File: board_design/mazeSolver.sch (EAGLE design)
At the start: 12 parts, among them IC1 L293DD, IC2 CP2101, J1 1-2295018-2, U1 ESP-WROOM-32, U2 AP1509-SOP8L

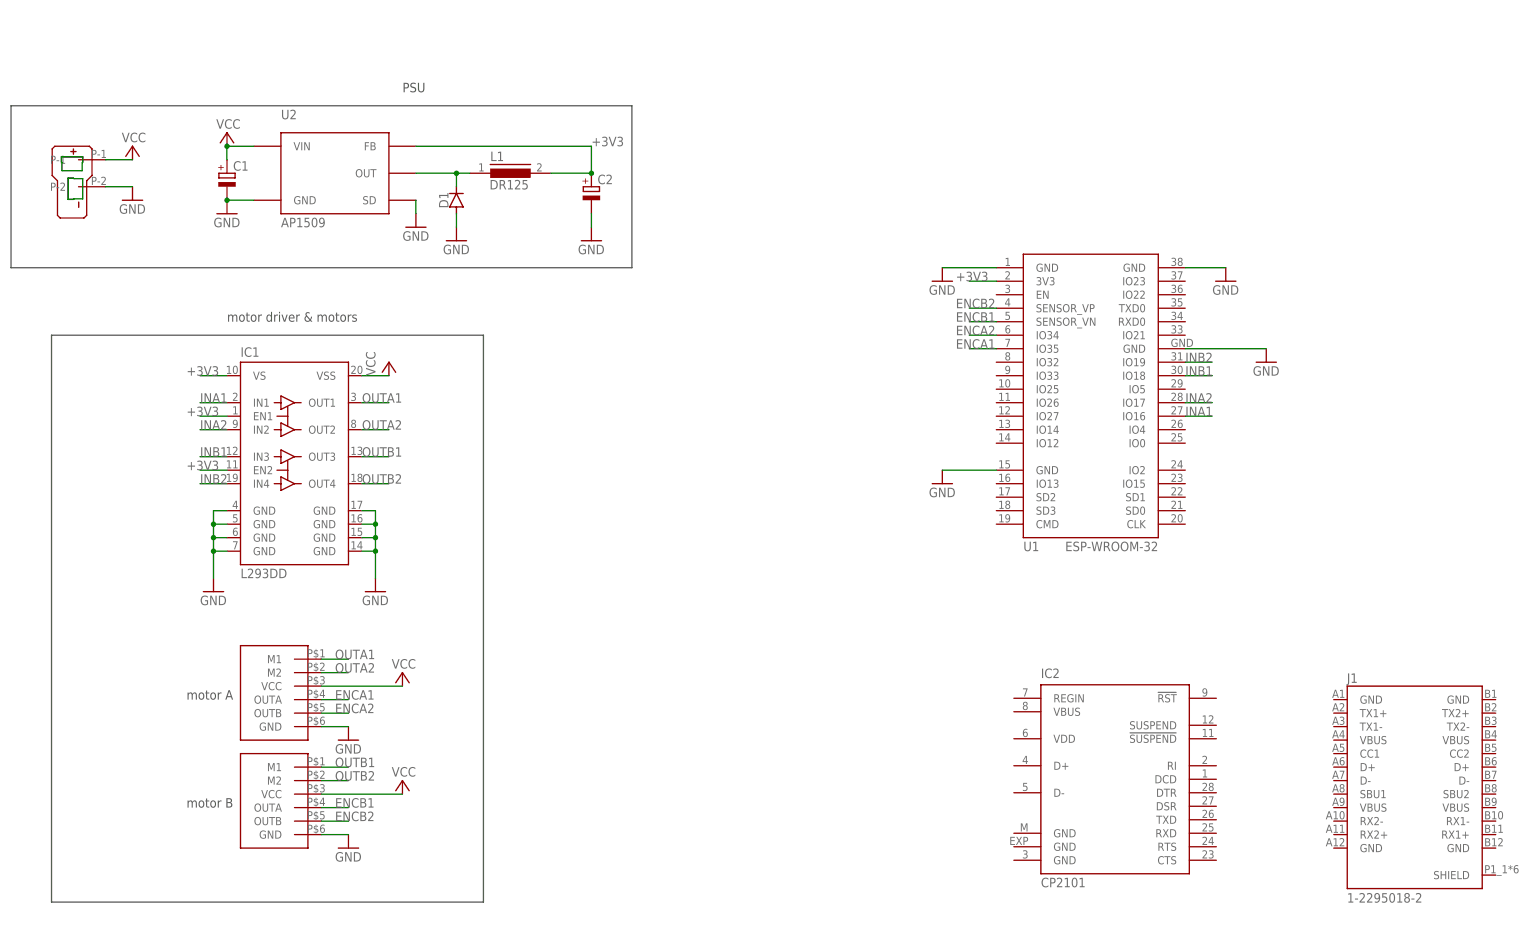
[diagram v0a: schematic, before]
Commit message: USB and reset circuitry.
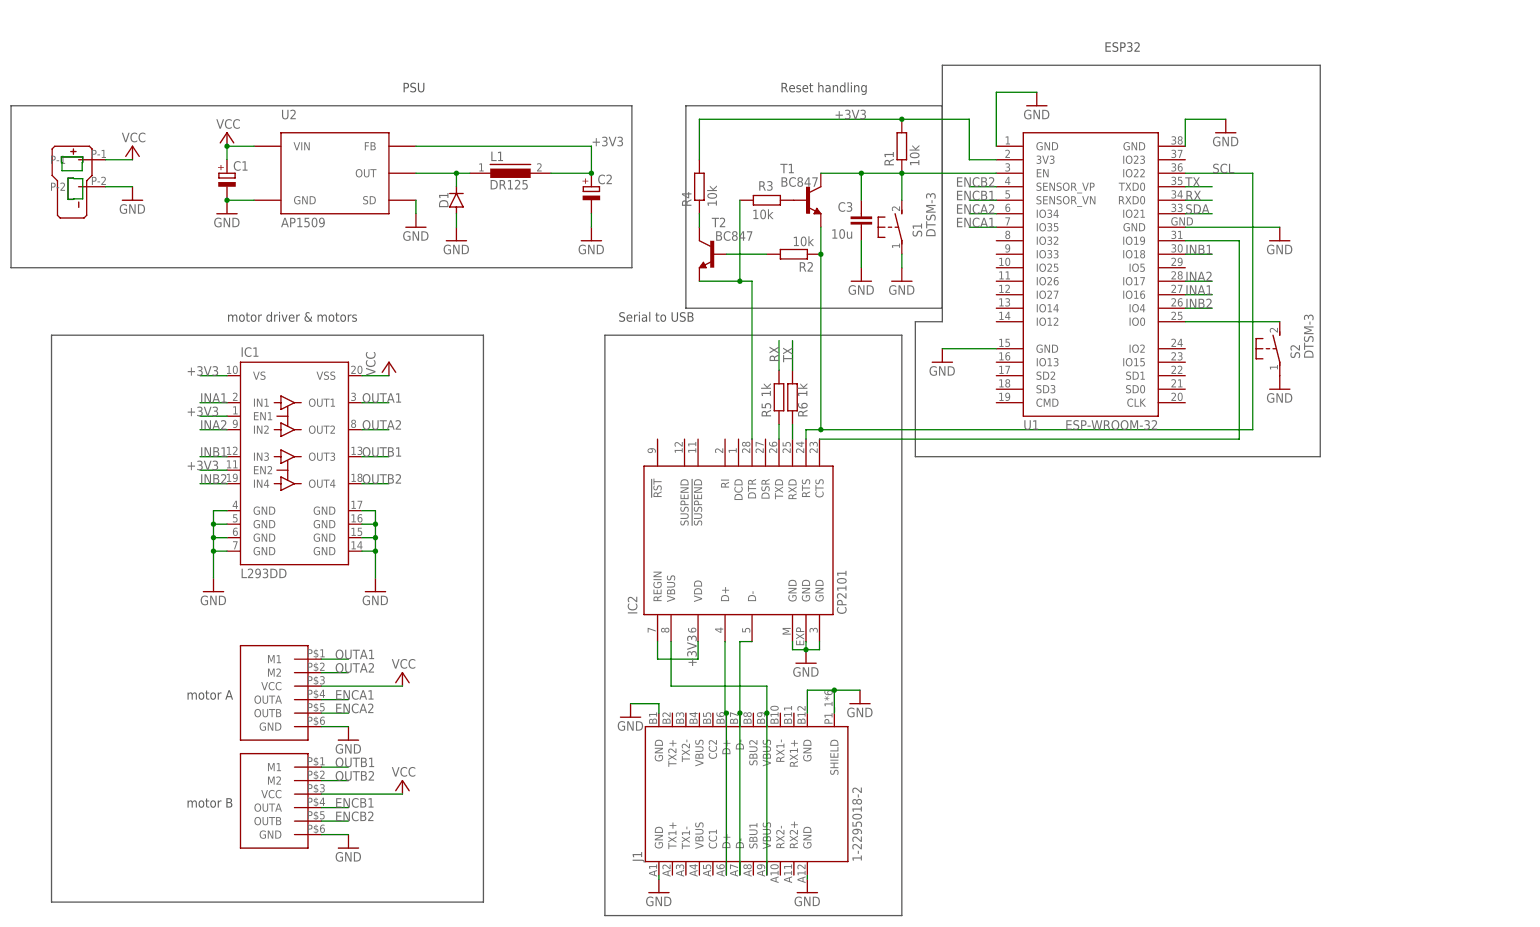
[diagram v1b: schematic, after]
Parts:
- added C3: 10u, rcl:C-EUC1206
- added R1, R2, R3, R4: 10k, rcl:R-EU_R1206
- added R5, R6: 1k, rcl:R-EU_R1206
- added S1, S2: DTSM-3, switch-tact:DTSM-3
- added T1, T2: BC847, transistor:BC847
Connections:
- new net N$1: C3.1, R1.1, S1.2, T1.C, U1.EN
- new net N$10: IC2.D+, J1.D+, J1.D+@1
- new net N$11: IC2.VBUS, J1.VBUS@2, J1.VBUS@4
- new net N$12: IC2.CTS, U1.IO19
- new net N$13: S2.2, U1.IO0
- new net N$2: R3.1, T1.B
- new net N$4: IC2.D-, J1.D-, J1.D-@1
- new net N$5: R2.2, T2.B
- new net N$6: R4.1, T2.C
- new net N$7: IC2.DTR, R3.2, T2.E
- new net N$8: IC2.TXD, R5.1
- new net N$9: IC2.RXD, R6.1
- new net RX: R5.2, U1.RXD0
- new net SCL: IC2.RTS, R2.1, T1.E, U1.IO22
- new net SDA: U1.IO21
- new net TX: R6.2, U1.TXD0
- net +3V3: now also IC2.REGIN, IC2.VDD, R1.2, R4.2
- net GND: now also C3.2, IC2.GND, IC2.GND@EXP, IC2.GND@M, J1.GND@1, J1.GND@2, J1.GND@3, J1.GND@4, J1.SHIELD, S1.1, S2.1
- net INB2: now also U1.IO4; no longer U1.IO19
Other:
- note added: "ESP32"
- note added: "Reset handling"
- note added: "Serial to USB"
- moved on the sheet: IC2, J1, U1

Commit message: Finished schematic
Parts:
- removed C3: 10u, rcl:C-EUC1206
- removed IC2: CP2101, silabs-2:CP2101
- removed J1: 1-2295018-2, 1-2295018-2:1-2295018-2
- removed R1, R2, R3, R4: 10k, rcl:R-EU_R1206
- removed R5, R6: 1k, rcl:R-EU_R1206
- removed S1, S2: DTSM-3, switch-tact:DTSM-3
- removed T1, T2: BC847, transistor:BC847
- removed U1: ESP-WROOM-32, esp32:ESP-WROOM-32
- added C4: 10u, rcl:C-EUC1206
- added IC3: CP2101, silabs-2:CP2101
- added J2: 1-2295018-2, 1-2295018-2:1-2295018-2
- added R10, R7, R8, R9: 10k, rcl:R-EU_R1206
- added R11, R12: 1k, rcl:R-EU_R1206
- added S3, S4: DTSM-3, switch-tact:DTSM-3
- added T3, T4: BC847, transistor:BC847
- added U$4: TDA9548, tda9548:TDA9548
- added U$5, U$6, U$7: VL6180X, vl6180x:VL6180X
- added U3: ESP-WROOM-32, esp32:ESP-WROOM-32
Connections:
- removed net N$10: IC2.D+, J1.D+, J1.D+@1
- removed net N$11: IC2.VBUS, J1.VBUS@2, J1.VBUS@4
- removed net N$12: IC2.CTS, U1.IO19
- removed net N$13: S2.2, U1.IO0
- removed net N$8: IC2.TXD, R5.1
- removed net N$9: IC2.RXD, R6.1
- new net N$14: C4.1, R7.1, S3.2, T3.C, U3.EN
- new net N$15: R9.1, T3.B
- new net N$16: R8.2, T4.B
- new net N$17: R10.1, T4.C
- new net N$18: IC3.DTR, R9.2, T4.E
- new net N$19: IC3.TXD, R11.1
- new net N$20: IC3.RXD, R12.1
- new net N$21: IC3.CTS, U3.IO19
- new net N$22: IC3.D-, J2.D-, J2.D-@1
- new net N$23: IC3.D+, J2.D+, J2.D+@1
- new net N$24: IC3.VBUS, J2.VBUS@2, J2.VBUS@4
- new net N$25: S4.2, U3.IO0
- net +3V3: now also IC3.REGIN, IC3.VDD, R10.2, R7.2, U$5.VCC, U$6.VCC, U$7.VCC, U3.3V3; no longer IC2.REGIN, IC2.VDD, R1.2, R4.2, U1.3V3
- net ENCA1: now also U3.IO35; no longer U1.IO35
- net ENCA2: now also U3.IO34; no longer U1.IO34
- net ENCB1: now also U3.SENSOR_VN; no longer U1.SENSOR_VN
- net ENCB2: now also U3.SENSOR_VP; no longer U1.SENSOR_VP
- net GND: now also C4.2, IC3.GND, IC3.GND@EXP, IC3.GND@M, J2.GND@1, J2.GND@2, J2.GND@3, J2.GND@4, J2.SHIELD, S3.1, S4.1, U$4.A0, U$4.A1, U$4.A2, U$4.GND, U$4.RST, U$5.GND, U$6.GND, U$7.GND, U3.GND@1, U3.GND@2, U3.GND@3, U3.GND@4; no longer C3.2, IC2.GND, IC2.GND@EXP, IC2.GND@M, J1.GND@1, J1.GND@2, J1.GND@3, J1.GND@4, J1.SHIELD, S1.1, S2.1, U1.GND@1, U1.GND@2, U1.GND@3, U1.GND@4
- net INA1: now also U3.IO16; no longer U1.IO16
- net INA2: now also U3.IO17; no longer U1.IO17
- net INB1: now also U3.IO18; no longer U1.IO18
- net INB2: now also U3.IO4; no longer U1.IO4
- net N$1: now also U$4.SC0, U$7.SCL; no longer C3.1, R1.1, S1.2, T1.C, U1.EN
- net N$2: now also U$4.SD0, U$7.SDA; no longer R3.1, T1.B
- net N$4: now also U$4.SD1, U$6.SDA; no longer IC2.D-, J1.D-, J1.D-@1
- net N$5: now also U$4.SC1, U$6.SCL; no longer R2.2, T2.B
- net N$6: now also U$4.SD2, U$5.SDA; no longer R4.1, T2.C
- net N$7: now also U$4.SC2, U$5.SCL; no longer IC2.DTR, R3.2, T2.E
- net RX: now also R11.2, U3.RXD0; no longer R5.2, U1.RXD0
- net SCL: now also IC3.RTS, R8.1, T3.E, U$4.SCL, U3.IO22; no longer IC2.RTS, R2.1, T1.E, U1.IO22
- net SDA: now also U$4.SDA, U3.IO21; no longer U1.IO21
- net TX: now also R12.2, U3.TXD0; no longer R6.2, U1.TXD0
- net VCC: now also U$4.VCC
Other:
- note added: "ESP32 & USB to TTL"
- note added: "I2C sensors"
- note added: "PSU & motor driver"

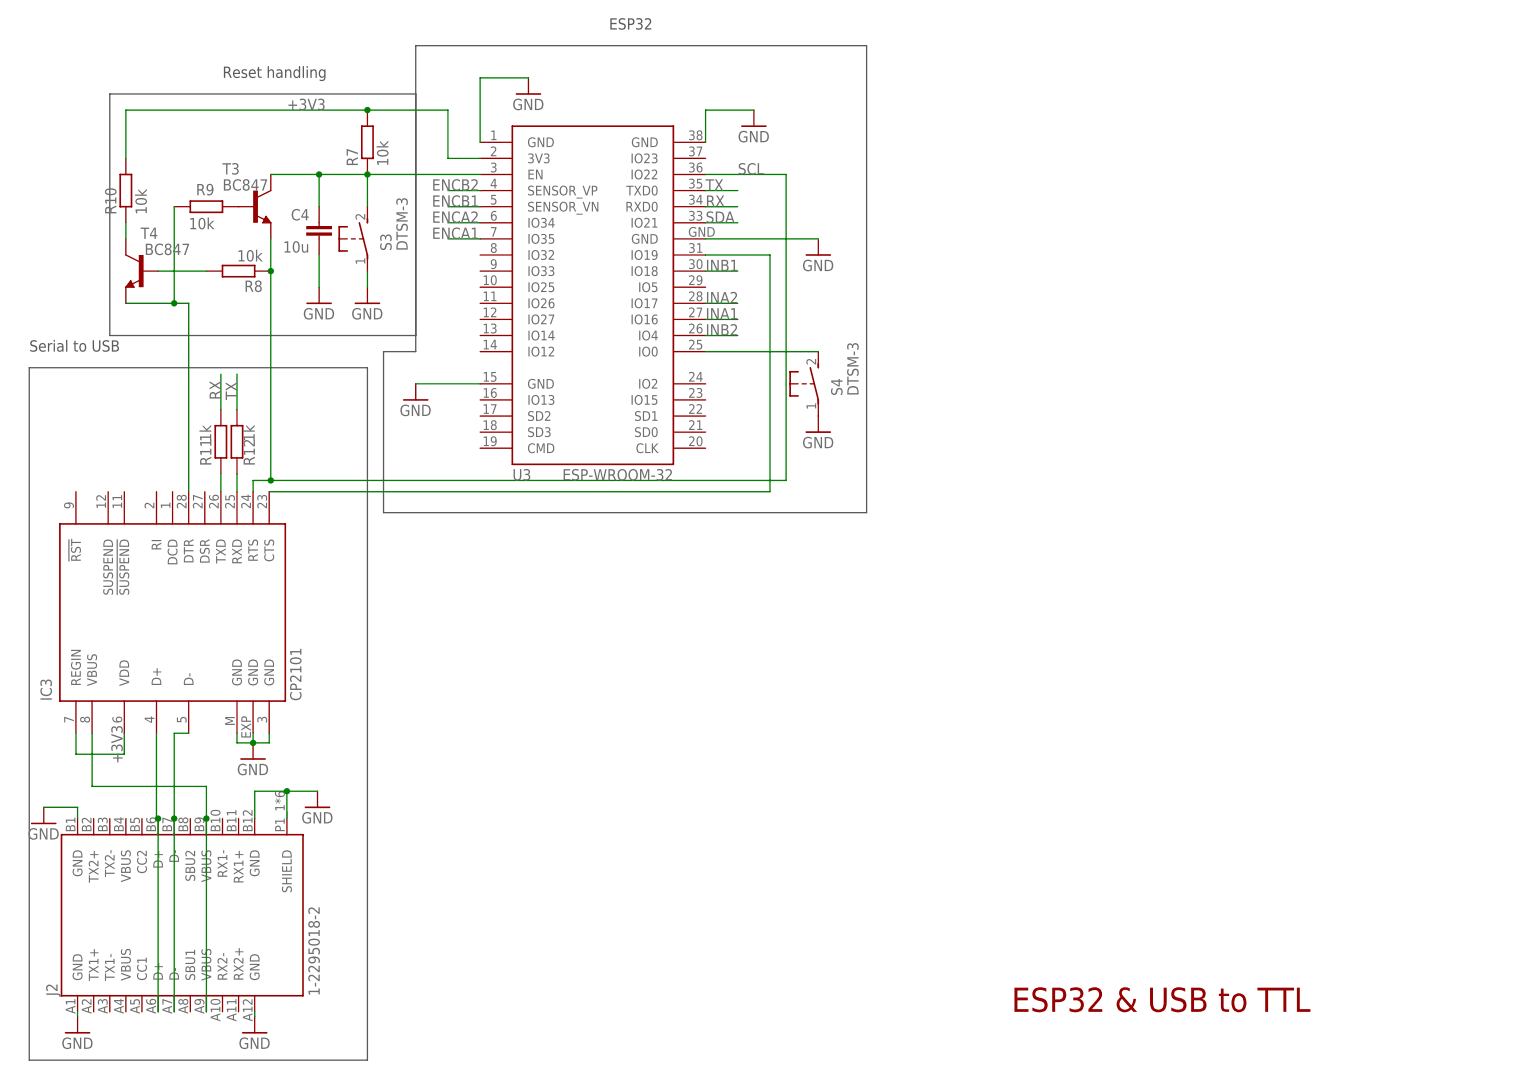
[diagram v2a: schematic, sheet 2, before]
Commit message: ESP32 circuit reworked.
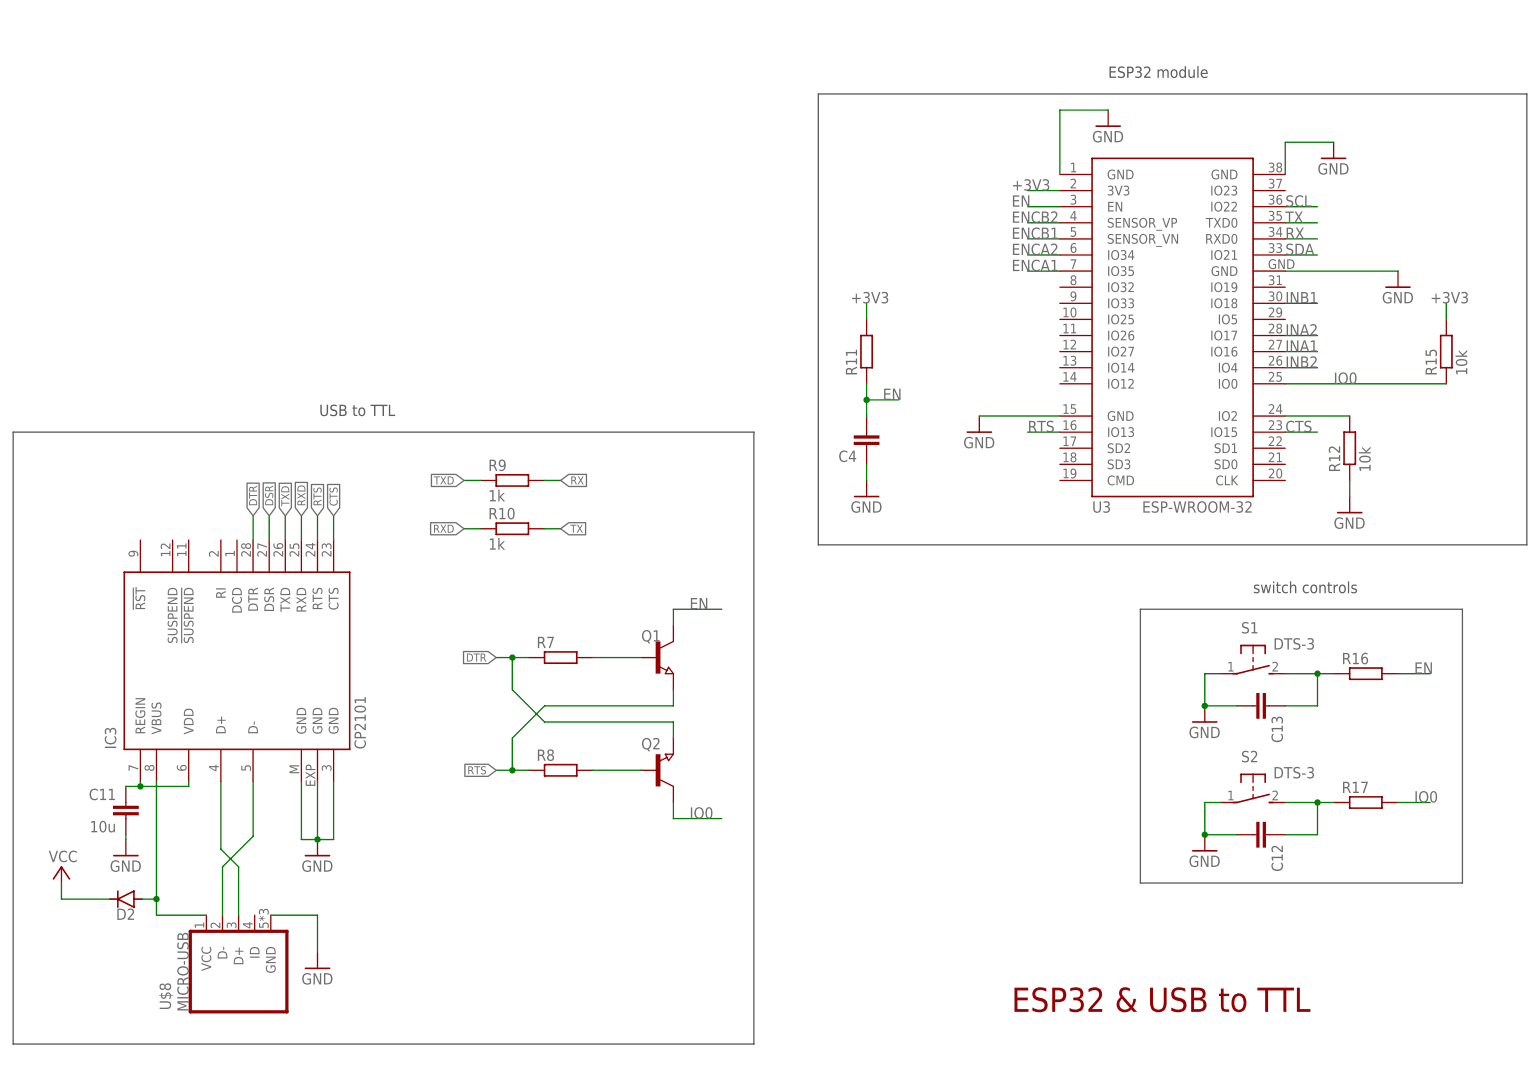
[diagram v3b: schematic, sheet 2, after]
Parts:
- removed J2: 1-2295018-2, 1-2295018-2:1-2295018-2
- removed S3, S4: DTSM-3, switch-tact:DTSM-3
- removed T3, T4: BC847, transistor:BC847
- added C10, C7, C8, C9: 22u, rcl:C-EUC1206
- added C11: 10u, rcl:C-EUC1206
- added C12, C13: (no value), rcl:C-EUC1206
- added C3: 10n, rcl:C-EUC1206
- added C5, C6: 100n, rcl:C-EUC1206
- added D2: (no value), diode:DIODE-DO214AC
- added Q1, Q2: (no value), semicon-smd-ipc:NPN-TRANSISTOR_SOT23
- added R1, R13, R14, R2, R3, R4, R5, R6: 4k7, rcl:R-EU_R1206
- added R15: 10k, rcl:R-EU_R1206
- added R16, R17: (no value), rcl:R-EU_R1206
- added S1, S2: DTS-3, switch-tact:DTS-3
- added U$8: MICRO-USB, microusb:MICRO-USB
- added U1: MPU-9250, MPU-9250:MPU-9250
- C4: value 10u -> (none)
- R10, R9: value 10k -> 1k
- R11: value 1k -> (none)
- R12: value 1k -> 10k
- R7, R8: value 10k -> (none)
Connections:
- removed net N$17: R10.1, T4.C
- removed net N$18: IC3.DTR, R9.2, T4.E
- removed net N$19: IC3.TXD, R11.1
- removed net N$20: IC3.RXD, R12.1
- removed net N$21: IC3.CTS, U3.IO19
- removed net N$23: IC3.D+, J2.D+, J2.D+@1
- removed net N$24: IC3.VBUS, J2.VBUS@2, J2.VBUS@4
- removed net N$25: S4.2, U3.IO0
- new net CTS: IC3.CTS, U3.IO15
- new net DSR: IC3.DSR
- new net DTR: IC3.DTR, Q2.E, R7.1
- new net EN: C4.2, Q1.C, R11.1, R16.2, U3.EN
- new net INT: U1.INT
- new net IO0: Q2.C, R15.1, R17.2, U3.IO0
- new net N$10: D2.A, IC3.VBUS, U$8.VCC
- new net N$11: C11.1, IC3.REGIN, IC3.VDD
- new net N$12: Q1.B, R7.2
- new net N$13: Q2.B, R8.2
- new net N$8: IC3.D-, U$8.D-
- new net N$9: IC3.D+, U$8.D+
- new net RTS: IC3.RTS, Q1.E, R8.1, U3.IO13
- new net RXD: IC3.RXD, R10.1
- new net TXD: IC3.TXD, R9.1
- net +3V3: now also C10.1, C3.1, C5.1, C7.1, C8.1, C9.1, R1.2, R11.2, R13.2, R14.2, R15.2, R2.2, R3.2, R4.2, R5.2, R6.2, U$4.VCC, U1.VDD, U1.VDDIO; no longer IC3.REGIN, IC3.VDD, R10.2, R7.2
- net GND: now also C10.2, C11.2, C12.2, C13.2, C3.2, C4.1, C5.2, C6.2, C7.2, C8.2, C9.2, R12.1, S1.1, S2.1, U$8.GND, U1.AD0/SDO, U1.FSYNC, U1.GND; no longer C4.2, J2.GND@1, J2.GND@2, J2.GND@3, J2.GND@4, J2.SHIELD, S3.1, S4.1
- net N$1: now also R13.1
- net N$14: now also C13.1, R16.1, S1.2; no longer C4.1, R7.1, S3.2, T3.C, U3.EN
- net N$15: now also C12.1, R17.1, S2.2; no longer R9.1, T3.B
- net N$16: now also R12.2, U3.IO2; no longer R8.2, T4.B
- net N$2: now also R14.1
- net N$22: now also C6.1, U1.REGOUT; no longer IC3.D-, J2.D-, J2.D-@1
- net N$4: now also R6.1
- net N$5: now also R5.1
- net N$6: now also R4.1
- net N$7: now also R3.1
- net RX: now also R9.2; no longer R11.2
- net SCL: now also R1.1, U1.SCL/SCLK; no longer IC3.RTS, R8.1, T3.E
- net SDA: now also R2.1, U1.SDA/SDI
- net TX: now also R10.2; no longer R12.2
- net VCC: now also D2.C; no longer U$4.VCC
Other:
- note added: "ESP32 module"
- note added: "IMU"
- note added: "USB to TTL"
- note added: "distance sensors"
- note added: "switch controls"
- note removed: "ESP32"
- note removed: "Reset handling"
- note removed: "Serial to USB"
- moved on the sheet: C1, C2, C4, D1, IC1, IC3, L1, R10, R11, R12, R7, R8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

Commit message: Final changes.
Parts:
- added IC2: 7805TV, linear:7805TV
- added SV1: (no value), con-lstb:MA04-1
- added U4: GY-521MPU6050, gy-521:GY-521MPU6050
- C1: value (none) -> 100u
- C2: value (none) -> 470u
- C4: value (none) -> 100n
- Q1, Q2: value (none) -> BC547
- R11: value (none) -> 10k
- R16, R17, R7, R8: value (none) -> 1k
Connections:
- net +3V3: now also IC2.VO, SV1.4, U4.VCC
- net GND: now also IC2.GND, SV1.1, U4.GND
- net INT: now also U3.IO25, U4.INT
- net RXD: now also SV1.2
- net SCL: now also U4.SCL
- net SDA: now also U4.SDA
- net TXD: now also SV1.3
- net VCC: now also IC2.VI
